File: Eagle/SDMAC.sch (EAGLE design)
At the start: 6 parts, among them IC1 SUPER_DMAC_THT, J1 CORTEX_DEBUG_PTH, U1 XC95288XL-10TQG144C, U2 NCP1117ST33T3G

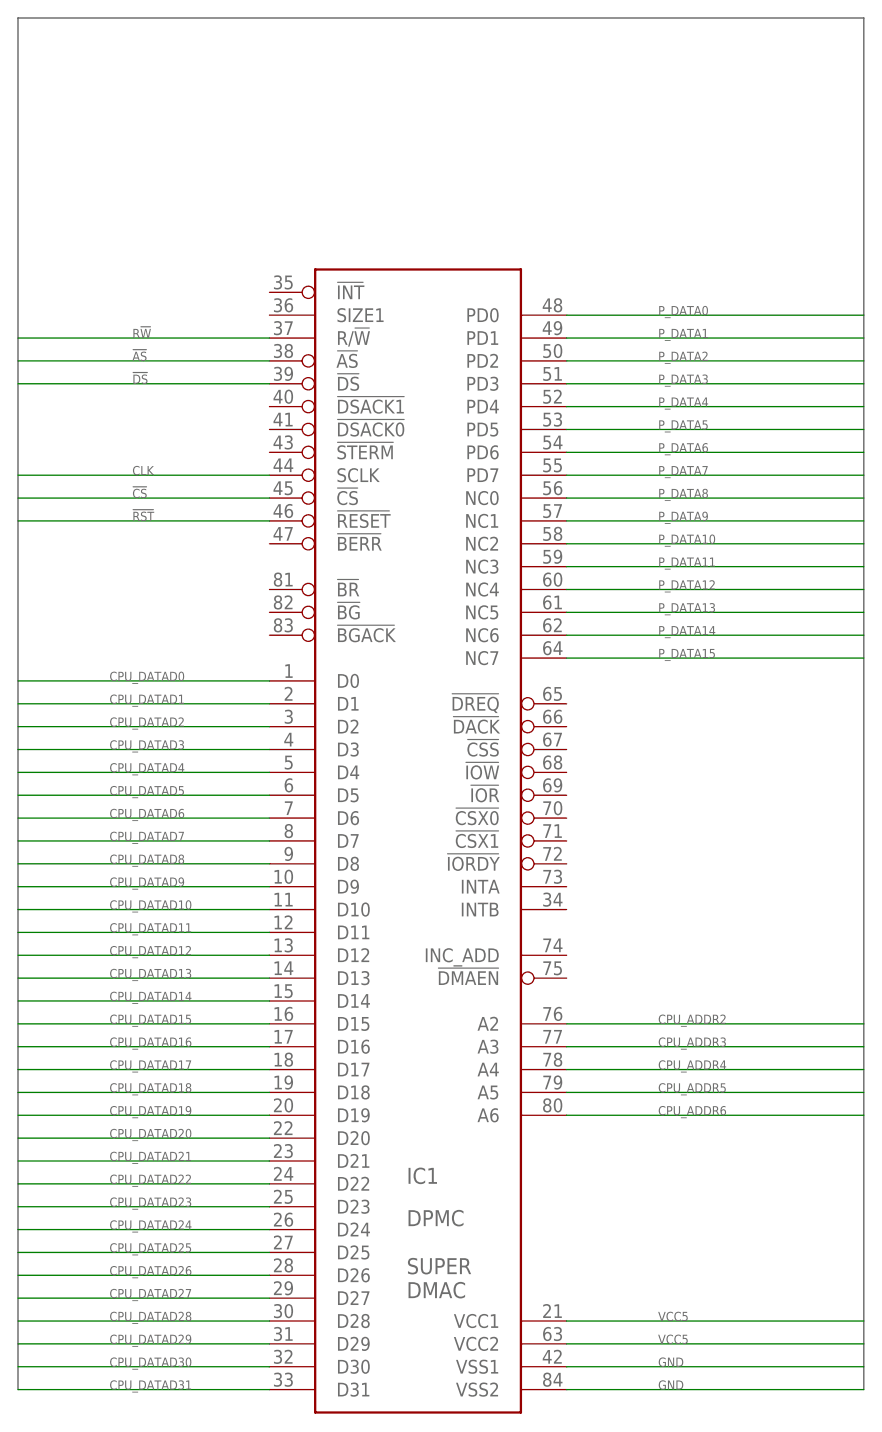
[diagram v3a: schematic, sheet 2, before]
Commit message: Routed more singnals and added example timing diagam to SDMAC.md
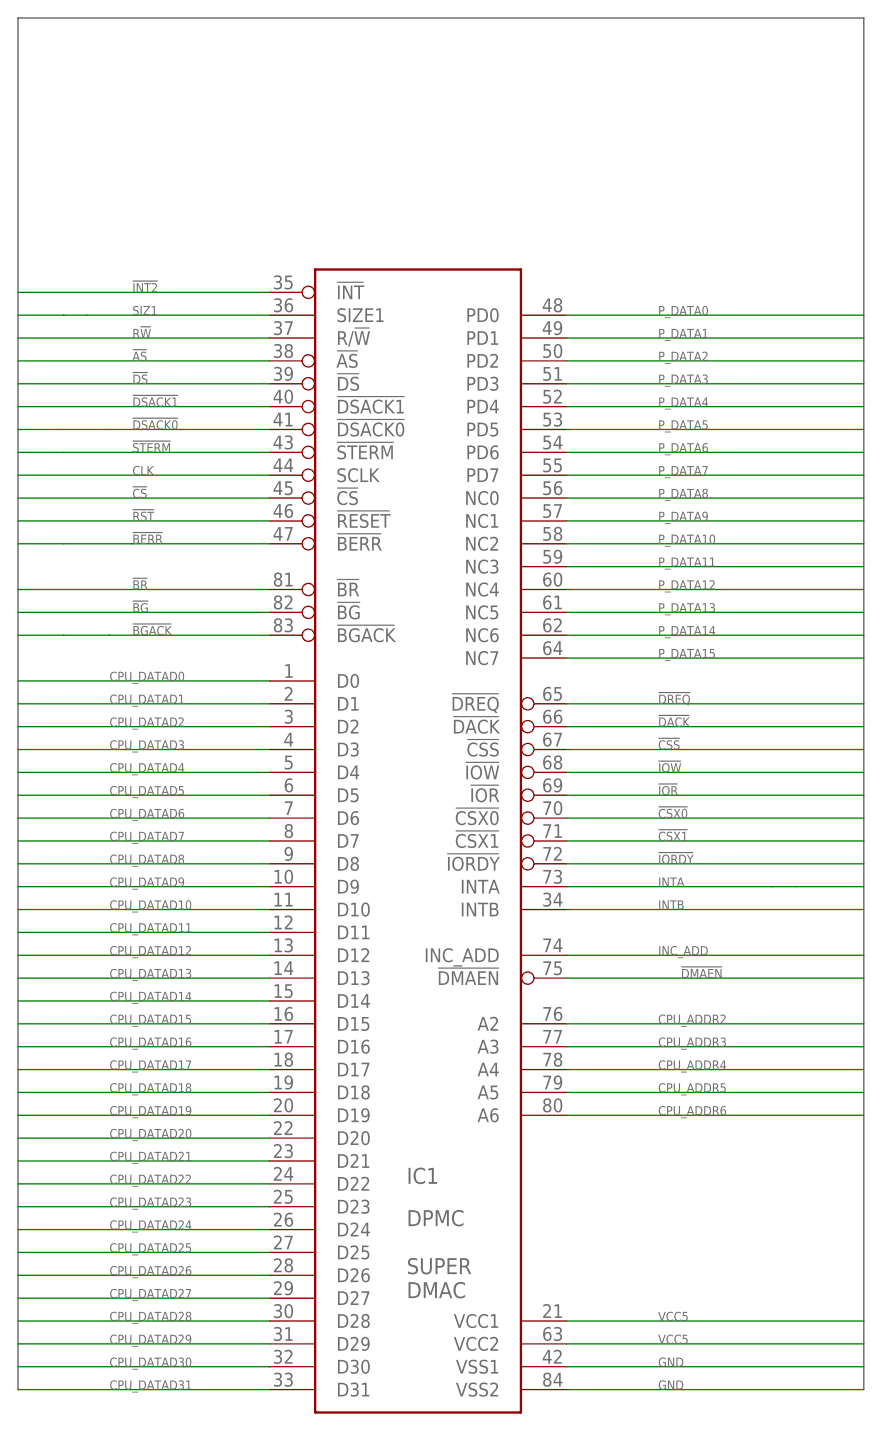
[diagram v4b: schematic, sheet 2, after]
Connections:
- new net !BERR: IC1.!BERR, U1B.NC_40
- new net !BG: IC1.!BG
- new net !BGACK: IC1.!BGACK
- new net !BR: IC1.!BR
- new net !CSS: IC1.!CSS
- new net !CSX0: IC1.!CSX0
- new net !CSX1: IC1.!CSX1
- new net !DACK: IC1.!DACK
- new net !DMAEN: IC1.!DMAEN
- new net !DREQ: IC1.!DREQ
- new net !DSACK0: IC1.!DSACK0, U1B.NC_45
- new net !DSACK1: IC1.!DSACK1, U1B.NC_46
- new net !INT2: IC1.!INT, U1B.NC_51
- new net !IOR: IC1.!IOR
- new net !IORDY: IC1.!IORDY
- new net !IOW: IC1.!IOW
- new net !STERM: IC1.!STERM, U1B.NC_44
- new net INC_ADD: IC1.INC_ADD
- new net INTA: IC1.INTA
- new net INTB: IC1.INTB
- new net SIZ1: IC1.SIZE1, U1B.NC_50
- net !AS: now also U1B.NC_48
- net !CS: now also U1B.NC_42; no longer U1B.NC_41
- net !DS: now also U1B.NC_47
- net !RST: now also U1B.NC_41; no longer U1B.NC_40
- net CLK: now also U1B.NC_43
- net R!W: now also U1B.NC_49

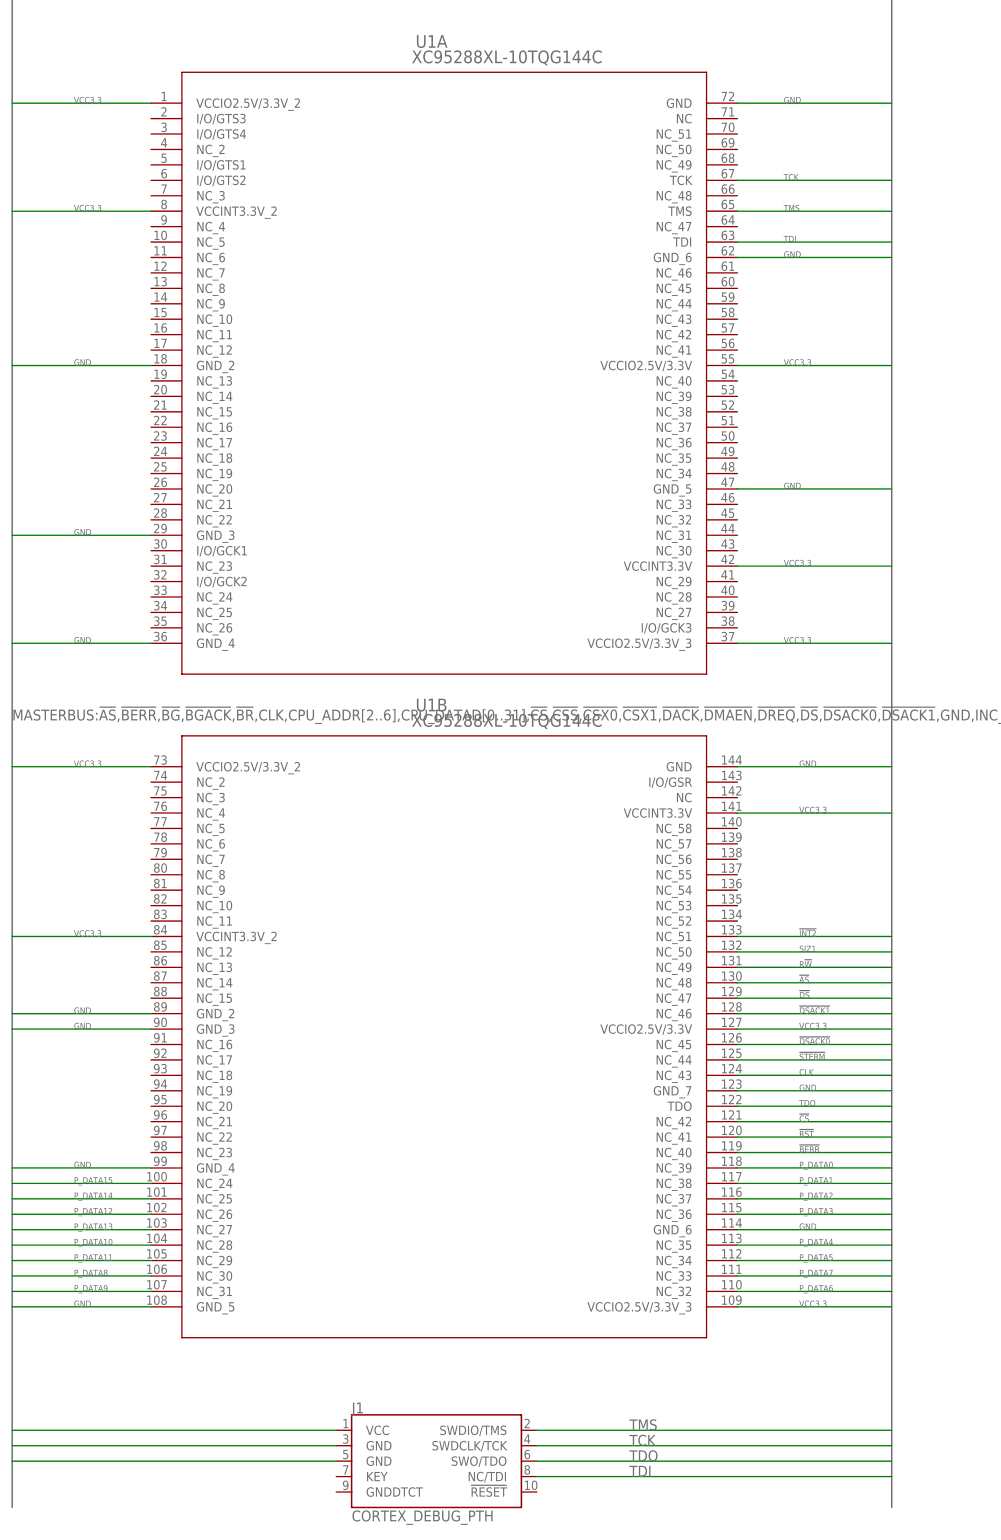
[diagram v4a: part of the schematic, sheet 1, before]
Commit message: Finished Initial Routing of signals in PCB design
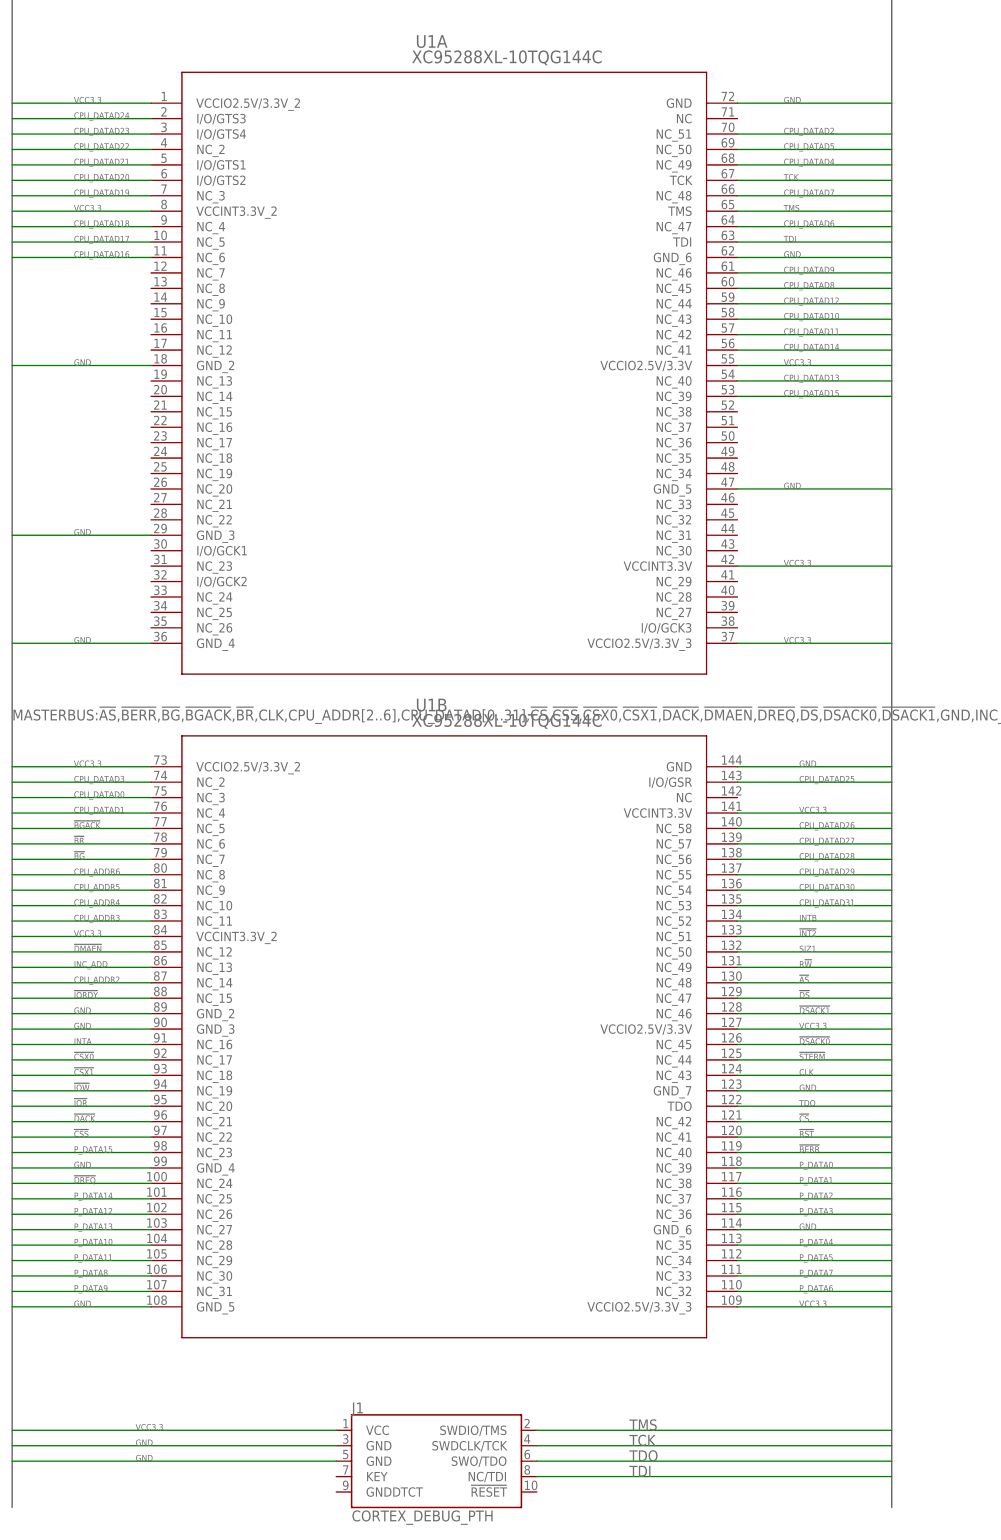
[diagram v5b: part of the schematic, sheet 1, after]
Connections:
- net !BG: now also U1B.NC_7
- net !BGACK: now also U1B.NC_5
- net !BR: now also U1B.NC_6
- net !CSS: now also U1B.NC_22
- net !CSX0: now also U1B.NC_17
- net !CSX1: now also U1B.NC_18
- net !DACK: now also U1B.NC_21
- net !DMAEN: now also U1B.NC_12
- net !DREQ: now also U1B.NC_24
- net !IOR: now also U1B.NC_20
- net !IORDY: now also U1B.NC_15
- net !IOW: now also U1B.NC_19
- net CPU_ADDR2: now also U1B.NC_14
- net CPU_ADDR3: now also U1B.NC_11
- net CPU_ADDR4: now also U1B.NC_10
- net CPU_ADDR5: now also U1B.NC_9
- net CPU_ADDR6: now also U1B.NC_8
- net CPU_DATAD0: now also U1B.NC_3
- net CPU_DATAD1: now also U1B.NC_4
- net CPU_DATAD10: now also U1A.NC_43
- net CPU_DATAD11: now also U1A.NC_42
- net CPU_DATAD12: now also U1A.NC_44
- net CPU_DATAD13: now also U1A.NC_40
- net CPU_DATAD14: now also U1A.NC_41
- net CPU_DATAD15: now also U1A.NC_39
- net CPU_DATAD16: now also U1A.NC_6
- net CPU_DATAD17: now also U1A.NC_5
- net CPU_DATAD18: now also U1A.NC_4
- net CPU_DATAD19: now also U1A.NC_3
- net CPU_DATAD2: now also U1A.NC_51
- net CPU_DATAD20: now also U1A.I/O/GTS2
- net CPU_DATAD21: now also U1A.I/O/GTS1
- net CPU_DATAD22: now also U1A.NC_2
- net CPU_DATAD23: now also U1A.I/O/GTS4
- net CPU_DATAD24: now also U1A.I/O/GTS3
- net CPU_DATAD25: now also U1B.I/O/GSR
- net CPU_DATAD26: now also U1B.NC_58
- net CPU_DATAD27: now also U1B.NC_57
- net CPU_DATAD28: now also U1B.NC_56
- net CPU_DATAD29: now also U1B.NC_55
- net CPU_DATAD3: now also U1B.NC_2
- net CPU_DATAD30: now also U1B.NC_54
- net CPU_DATAD31: now also U1B.NC_53
- net CPU_DATAD4: now also U1A.NC_49
- net CPU_DATAD5: now also U1A.NC_50
- net CPU_DATAD6: now also U1A.NC_47
- net CPU_DATAD7: now also U1A.NC_48
- net CPU_DATAD8: now also U1A.NC_45
- net CPU_DATAD9: now also U1A.NC_46
- net INC_ADD: now also U1B.NC_13
- net INTA: now also U1B.NC_16
- net INTB: now also U1B.NC_52
- net P_DATA15: now also U1B.NC_23; no longer U1B.NC_24

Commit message: PCB Design Finished
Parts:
- removed C2: 10uF, Capacitor:C_CHIP-0805(2012-METRIC)
- removed J1: CORTEX_DEBUG_PTH, SparkFun-Connectors:CORTEX_DEBUG_PTH
- added A12: (no value), jumper:JP1E
- added C10, C11, C12, C3, C4, C5, C6, C7, C8, C9: 0.1uF, Capacitor:C_CHIP-0805(2012-METRIC)
- added C13: 10uF, Volks73-Kemet:T491A106K010AT
- added DMA, PWR, RD, WR: (no value), led:LEDSML0805
- added R1, R2, R3, R4: 430, rcl:R-EU_R0805
- added SV1: (no value), con-lstb:MA06-1
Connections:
- new net A12: A12.2, U1A.NC_10
- new net DMA_LED: DMA.C, U1A.NC_9
- new net N$1: PWR.A, R1.2
- new net N$2: R2.2, WR.A
- new net N$3: R3.2, RD.A
- new net N$4: DMA.A, R4.2
- new net RD_LED: RD.C, U1A.NC_8
- new net WR_LED: U1A.NC_7, WR.C
- net GND: now also A12.1, C10.2, C11.2, C12.2, C13.C, C3.2, C4.2, C5.2, C6.2, C7.2, C8.2, C9.2, PWR.C, SV1.5; no longer C2.2, J1.GND@3, J1.GND@5
- net TCK: now also SV1.4; no longer J1.SWDCLK/TCK
- net TDI: now also SV1.2; no longer J1.NC/TDI
- net TDO: now also SV1.3; no longer J1.SWO/TDO
- net TMS: now also SV1.1; no longer J1.SWDIO/TMS
- net VCC3.3: now also C10.1, C11.1, C12.1, C13.A, C3.1, C4.1, C5.1, C6.1, C7.1, C8.1, C9.1, R1.1, R2.1, R3.1, R4.1, SV1.6; no longer C2.1, J1.VCC

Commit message: updated makefile, schmatics, gerbers etc...
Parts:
- added 5V: (no value), jumper:JP1E
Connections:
- net !AS: now also U1A.I/O/GCK2; no longer U1B.NC_48
- net !CS: now also U1A.I/O/GTS4; no longer U1B.NC_42
- net !DS: now also U1A.I/O/GCK3; no longer U1B.NC_47
- net !RST: now also U1B.I/O/GSR; no longer U1B.NC_41
- net CLK: now also U1A.I/O/GCK1; no longer U1B.NC_43
- net CPU_DATAD23: now also U1A.NC_12; no longer U1A.I/O/GTS4
- net CPU_DATAD24: now also U1A.NC_11; no longer U1A.I/O/GTS3
- net CPU_DATAD25: now also U1B.NC; no longer U1B.I/O/GSR
- net GND: now also 5V.1
- net R!W: now also U1A.I/O/GTS3; no longer U1B.NC_49
- net VCC5: now also 5V.2
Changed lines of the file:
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@@
 <attribute name="SPICEPREFIX" value="X"/>
 </part>
+<part name="5V" library="jumper" library_urn="urn:adsk.eagle:library:252" deviceset="JP1E" device="" package3d_urn="urn:adsk.eagle:package:15455/1"/>
 </parts>
 <sheets>
@@
 <net name="!CS" class="0">
 <segment>
-<pinref part="U1" gate="B" pin="NC_42"/>
-<wire x1="160.02" y1="-83.82" x2="134.62" y2="-83.82" width="0.1524" layer="91"/>
-<label x="144.78" y="-83.82" size="1.016" layer="95"/>
+<pinref part="U1" gate="A" pin="I/O/GTS4"/>
+<wire x1="38.1" y1="78.74" x2="15.24" y2="78.74" width="0.1524" layer="91"/>
+<label x="25.4" y="78.74" size="1.016" layer="95"/>
 </segment>
 </net>
 <net name="!RST" class="0">
 <segment>
-<pinref part="U1" gate="B" pin="NC_41"/>
-<wire x1="134.62" y1="-86.36" x2="160.02" y2="-86.36" width="0.1524" layer="91"/>
-<label x="144.78" y="-86.36" size="1.016" layer="95"/>
+<pinref part="U1" gate="B" pin="I/O/GSR"/>
+<wire x1="134.62" y1="-27.94" x2="160.02" y2="-27.94" width="0.1524" layer="91"/>
+<label x="144.78" y="-27.94" size="1.016" layer="95"/>
 </segment>
 </net>
@@
 <net name="CLK" class="0">
 <segment>
-<pinref part="U1" gate="B" pin="NC_43"/>
-<wire x1="134.62" y1="-76.2" x2="160.02" y2="-76.2" width="0.1524" layer="91"/>
-<label x="144.78" y="-76.2" size="1.016" layer="95"/>
+<pinref part="U1" gate="A" pin="I/O/GCK1"/>
+<wire x1="38.1" y1="10.16" x2="15.24" y2="10.16" width="0.1524" layer="91"/>
+<label x="25.4" y="12.7" size="1.016" layer="95"/>
+<label x="25.4" y="10.16" size="1.016" layer="95"/>
 </segment>
 </net>
@@
 <net name="!DS" class="0">
 <segment>
-<pinref part="U1" gate="B" pin="NC_47"/>
-<wire x1="134.62" y1="-63.5" x2="160.02" y2="-63.5" width="0.1524" layer="91"/>
-<label x="144.78" y="-63.5" size="1.016" layer="95"/>
+<pinref part="U1" gate="A" pin="I/O/GCK3"/>
+<wire x1="134.62" y1="-2.54" x2="160.02" y2="-2.54" width="0.1524" layer="91"/>
+<label x="142.24" y="-2.54" size="1.016" layer="95"/>
 </segment>
 </net>
 <net name="!AS" class="0">
 <segment>
-<pinref part="U1" gate="B" pin="NC_48"/>
-<wire x1="134.62" y1="-60.96" x2="160.02" y2="-60.96" width="0.1524" layer="91"/>
-<label x="144.78" y="-60.96" size="1.016" layer="95"/>
+<pinref part="U1" gate="A" pin="I/O/GCK2"/>
+<wire x1="38.1" y1="5.08" x2="15.24" y2="5.08" width="0.1524" layer="91"/>
+<label x="25.4" y="5.08" size="1.016" layer="95"/>
 </segment>
 </net>
 <net name="R!W" class="0">
 <segment>
-<pinref part="U1" gate="B" pin="NC_49"/>
-<wire x1="134.62" y1="-58.42" x2="160.02" y2="-58.42" width="0.1524" layer="91"/>
-<label x="144.78" y="-58.42" size="1.016" layer="95"/>
+<pinref part="U1" gate="A" pin="I/O/GTS3"/>
+<wire x1="38.1" y1="81.28" x2="15.24" y2="81.28" width="0.1524" layer="91"/>
+<label x="25.4" y="81.28" size="1.016" layer="95"/>
 </segment>
 </net>
@@
 <net name="CPU_DATAD25" class="0">
 <segment>
-<pinref part="U1" gate="B" pin="I/O/GSR"/>
-<wire x1="134.62" y1="-27.94" x2="160.02" y2="-27.94" width="0.1524" layer="91"/>
-<label x="144.78" y="-27.94" size="1.016" layer="95"/>
+<pinref part="U1" gate="B" pin="NC"/>
+<wire x1="134.62" y1="-30.48" x2="160.02" y2="-30.48" width="0.1524" layer="91"/>
+<label x="144.78" y="-30.48" size="1.016" layer="95"/>
 </segment>
 </net>
 <net name="CPU_DATAD24" class="0">
 <segment>
-<pinref part="U1" gate="A" pin="I/O/GTS3"/>
-<wire x1="38.1" y1="81.28" x2="15.24" y2="81.28" width="0.1524" layer="91"/>
-<label x="25.4" y="81.28" size="1.016" layer="95"/>
-</segment>
-</net>
-<net name="CPU_DATAD23" class="0">
-<segment>
-<pinref part="U1" gate="A" pin="I/O/GTS4"/>
-<wire x1="38.1" y1="78.74" x2="15.24" y2="78.74" width="0.1524" layer="91"/>
-<label x="25.4" y="78.74" size="1.016" layer="95"/>
+<pinref part="U1" gate="A" pin="NC_11"/>
+<wire x1="38.1" y1="45.72" x2="15.24" y2="45.72" width="0.1524" layer="91"/>
+<label x="25.4" y="45.72" size="1.016" layer="95"/>
 </segment>
 </net>
@@
 <label x="25.4" y="48.26" size="1.016" layer="95"/>
 <wire x1="38.1" y1="48.26" x2="15.24" y2="48.26" width="0.1524" layer="91"/>
+</segment>
+</net>
+<net name="CPU_DATAD23" class="0">
+<segment>
+<pinref part="U1" gate="A" pin="NC_12"/>
+<wire x1="38.1" y1="43.18" x2="15.24" y2="43.18" width="0.1524" layer="91"/>
+<label x="25.4" y="43.18" size="1.016" layer="95"/>
 </segment>
 </net>
@@
 <attribute name="VALUE" x="76.2" y="87.376" size="1.778" layer="96" rot="R90"/>
 </instance>
+<instance part="5V" gate="A" x="17.78" y="86.36" smashed="yes" rot="R90">
+<attribute name="NAME" x="17.78" y="85.09" size="1.778" layer="95" rot="R180"/>
+<attribute name="VALUE" x="17.78" y="92.075" size="1.778" layer="96" rot="R180"/>
+</instance>
 </instances>
 <busses>
@@
 <label x="27.94" y="99.06" size="1.778" layer="95" rot="R180" xref="yes"/>
 <pinref part="C1" gate="G$1" pin="1"/>
-<wire x1="33.02" y1="99.06" x2="27.94" y2="99.06" width="0.1524" layer="91"/>
+<wire x1="33.02" y1="99.06" x2="30.48" y2="99.06" width="0.1524" layer="91"/>
+<wire x1="30.48" y1="99.06" x2="27.94" y2="99.06" width="0.1524" layer="91"/>
 <wire x1="33.02" y1="93.98" x2="33.02" y2="99.06" width="0.1524" layer="91"/>
 <junction x="33.02" y="99.06"/>
+<pinref part="5V" gate="A" pin="2"/>
+<wire x1="20.32" y1="88.9" x2="30.48" y2="88.9" width="0.1524" layer="91"/>
+<wire x1="30.48" y1="88.9" x2="30.48" y2="99.06" width="0.1524" layer="91"/>
+<junction x="30.48" y="99.06"/>
 </segment>
 </net>
@@
 <wire x1="71.12" y1="86.36" x2="71.12" y2="81.28" width="0.1524" layer="91"/>
 <junction x="71.12" y="81.28"/>
-</segment>
-<segment>
+<pinref part="5V" gate="A" pin="1"/>
+<wire x1="20.32" y1="86.36" x2="25.4" y2="86.36" width="0.1524" layer="91"/>
+<wire x1="25.4" y1="86.36" x2="25.4" y2="81.28" width="0.1524" layer="91"/>
+<wire x1="25.4" y1="81.28" x2="33.02" y2="81.28" width="0.1524" layer="91"/>
+<junction x="33.02" y="81.28"/>
+</segment>
+<segment>
